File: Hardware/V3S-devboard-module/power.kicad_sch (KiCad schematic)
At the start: 68 parts, among them U101 EA3036C, U102 XC6206PxxxMR

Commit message: layout
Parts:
- removed C105, C107, C109: 18p, Capacitor_SMD:C_0402_1005Metric, symbol Device:C_Small
- removed C106, C108, C110: 10u, Capacitor_SMD:C_0603_1608Metric, symbol Device:C_Small
- removed L101, L102, L103: 2.2u, Inductor_SMD:L_1008_2520Metric, symbol Device:L_Small
- removed NT10, NT11, NT12, NT13, NT2, NT3, NT4, NT5, NT6, NT7, NT8, NT9: NetTie_2, NetTie:NetTie-2_SMD_Pad0.5mm, symbol Device:NetTie_2
- removed R101, R102, R106: 150K, Resistor_SMD:R_0402_1005Metric, symbol Device:R_Small_US
- removed R103: 200K, Resistor_SMD:R_0402_1005Metric, symbol Device:R_Small_US
- removed R104: 100K, Resistor_SMD:R_0402_1005Metric, symbol Device:R_Small_US
- removed R105: 680K, Resistor_SMD:R_0402_1005Metric, symbol Device:R_Small_US
- added C1, C3, C5: 18p, Capacitor_SMD:C_0402_1005Metric, symbol Device:C_Small
- added C2, C4, C6: 10u, Capacitor_SMD:C_0603_1608Metric, symbol Device:C_Small
- added L1, L2, L3: 2.2u, Inductor_SMD:L_1008_2520Metric, symbol Device:L_Small
- added R1: 680K, Resistor_SMD:R_0402_1005Metric, symbol Device:R_Small_US
- added R2, R5, R6: 150K, Resistor_SMD:R_0402_1005Metric, symbol Device:R_Small_US
- added R3: 200K, Resistor_SMD:R_0402_1005Metric, symbol Device:R_Small_US
- added R4: 100K, Resistor_SMD:R_0402_1005Metric, symbol Device:R_Small_US
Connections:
- net VCC_DRAM is gone; now on net 1V8: C203.2, C204.2, C205.2, C206.2, C207.2, R201.1
- net VCC_HP is gone; now on net 3V3: C224.2
- net VCC_IO is gone; now on net 3V3: C216.2, C217.2, C218.2, C219.2
- net VCC_MSCI is gone; now on net 3V3: C221.2
- net VCC_PLL is gone; now on net 3V0: C223.2
- net VCC_USB is gone; now on net 3V3: C220.2
- net VDD_CPU is gone; now on net 1V2: C212.2, C213.2, C214.2, C215.2
- net VDD_SYS is gone; now on net 1V2: C208.2, C209.2, C210.2, C211.2
- net 1V2: now also C5.2, C6.2, L3.2, R5.1
- net 1V8: now also C3.2, C4.2, L2.2, R3.1
- net 3V3: now also C1.2, C2.2, L1.2, R1.1
- net GND: now also C2.1, C4.1, C6.1, R2.2, R4.2, R6.2
- net at U101.6 (LX2): now also L1.1
- net at U101.3 (FB2): now also C5.1, R5.2, R6.1
- net at U101.11 (LX1): now also L2.1
- net at U101.14 (FB1): now also C3.1, R3.2, R4.1
- net at U101.20 (LX3): now also L3.1
- net at U101.2 (FB3): now also C1.1, R1.2, R2.1

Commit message: layout
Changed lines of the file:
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@@
 				)
 				(justify left)
-				(hide yes)
 			)
 		)
@@
 					(size 1.27 1.27)
 				)
-				(hide yes)
 			)
 		)

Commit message: layout
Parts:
- added J1: Conn_01x02, Connector_PinHeader_2.54mm:PinHeader_1x02_P2.54mm_Vertical, symbol Connector_Generic:Conn_01x02
- U101: LCSC (none) -> C570857; LCSC Part C570857 -> (none)
- U102: LCSC (none) -> C5148691
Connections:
- net 5V: now also J1.1 (Pin_1)
- net GND: now also J1.2 (Pin_2)
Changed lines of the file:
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@@
 	)
 	(symbol
+		(lib_id "Connector_Generic:Conn_01x02")
+		(at 27.94 57.15 0)
+		(mirror y)
+		(unit 1)
+		(exclude_from_sim no)
+		(in_bom yes)
+		(on_board yes)
+		(dnp no)
+		(fields_autoplaced yes)
+		(property "Reference" "J1"
+			(at 27.94 50.8 0)
+			(effects
+				(font
+					(size 1.27 1.27)
+				)
+			)
+		)
+		(property "Value" "Conn_01x02"
+			(at 27.94 53.34 0)
+			(effects
+				(font
+					(size 1.27 1.27)
+				)
+			)
+		)
+		(property "Footprint" "Connector_PinHeader_2.54mm:PinHeader_1x02_P2.54mm_Vertical"
+			(at 27.94 57.15 0)
+			(effects
+				(font
+					(size 1.27 1.27)
+				)
+				(hide yes)
+			)
+		)
+		(property "Datasheet" "~"
+			(at 27.94 57.15 0)
+			(effects
+				(font
+					(size 1.27 1.27)
+				)
+				(hide yes)
+			)
+		)
+		(property "Description" "Generic connector, single row, 01x02, script generated (kicad-library-utils/schlib/autogen/connector/)"
+			(at 27.94 57.15 0)
+			(effects
+				(font
+					(size 1.27 1.27)
+				)
+				(hide yes)
+			)
+		)
+		(pin "1"
+		)
+		(pin "2"
+		)
+		(instances
+			(project "V3S-devboard-module"
+				(path "/5d41c08e-2331-42df-a2d5-1aeb6ed4388c/5949d9b7-76b3-40a2-8931-5cd58c7934ef"
+					(reference "J1")
+					(unit 1)
+				)
+			)
+		)
+	)
+	(symbol
 		(lib_id "power:GND")
 		(at 140.97 63.5 0)
@@
 			)
 		)
+		(property "LCSC" "C5148691"
+			(at 176.53 39.37 0)
+			(effects
+				(font
+					(size 1.27 1.27)
+				)
+				(hide yes)
+			)
+		)
 		(pin "2"
 		)
@@
 	)
 	(symbol
+		(lib_id "power:VCC")
+		(at 33.02 57.15 0)
+		(unit 1)
+		(exclude_from_sim no)
+		(in_bom yes)
+		(on_board yes)
+		(dnp no)
+		(property "Reference" "#PWR0108"
+			(at 33.02 60.96 0)
+			(effects
+				(font
+					(size 1.27 1.27)
+				)
+				(hide yes)
+			)
+		)
+		(property "Value" "5V"
+			(at 31.75 53.34 0)
+			(effects
+				(font
+					(size 1.27 1.27)
+				)
+				(justify left)
+			)
+		)
+		(property "Footprint" ""
+			(at 33.02 57.15 0)
+			(effects
+				(font
+					(size 1.27 1.27)
+				)
+				(hide yes)
+			)
+		)
+		(property "Datasheet" ""
+			(at 33.02 57.15 0)
+			(effects
+				(font
+					(size 1.27 1.27)
+				)
+				(hide yes)
+			)
+		)
+		(property "Description" "Power symbol creates a global label with name \"VCC\""
+			(at 33.02 57.15 0)
+			(effects
+				(font
+					(size 1.27 1.27)
+				)
+				(hide yes)
+			)
+		)
+		(pin "1"
+		)
+		(instances
+			(project "V3S-devboard-module"
+				(path "/5d41c08e-2331-42df-a2d5-1aeb6ed4388c/5949d9b7-76b3-40a2-8931-5cd58c7934ef"
+					(reference "#PWR0108")
+					(unit 1)
+				)
+			)
+		)
+	)
+	(symbol
 		(lib_id "Device:C_Small")
 		(at 147.32 144.78 180)
@@
 	)
 	(symbol
+		(lib_id "power:GND")
+		(at 33.02 59.69 0)
+		(unit 1)
+		(exclude_from_sim no)
+		(in_bom yes)
+		(on_board yes)
+		(dnp no)
+		(fields_autoplaced yes)
+		(property "Reference" "#PWR0122"
+			(at 33.02 66.04 0)
+			(effects
+				(font
+					(size 1.27 1.27)
+				)
+				(hide yes)
+			)
+		)
+		(property "Value" "GND"
+			(at 33.02 64.77 0)
+			(effects
+				(font
+					(size 1.27 1.27)
+				)
+			)
+		)
+		(property "Footprint" ""
+			(at 33.02 59.69 0)
+			(effects
+				(font
+					(size 1.27 1.27)
+				)
+				(hide yes)
+			)
+		)
+		(property "Datasheet" ""
+			(at 33.02 59.69 0)
+			(effects
+				(font
+					(size 1.27 1.27)
+				)
+				(hide yes)
+			)
+		)
+		(property "Description" "Power symbol creates a global label with name \"GND\" , ground"
+			(at 33.02 59.69 0)
+			(effects
+				(font
+					(size 1.27 1.27)
+				)
+				(hide yes)
+			)
+		)
+		(pin "1"
+		)
+		(instances
+			(project "V3S-devboard-module"
+				(path "/5d41c08e-2331-42df-a2d5-1aeb6ed4388c/5949d9b7-76b3-40a2-8931-5cd58c7934ef"
+					(reference "#PWR0122")
+					(unit 1)
+				)
+			)
+		)
+	)
+	(symbol
 		(lib_id "Device:C_Small")
 		(at 54.61 111.76 180)
@@
 			)
 		)
-		(property "LCSC Part" "C570857"
+		(property "LCSC" "C570857"
 			(at 78.74 81.28 0)
 			(effects

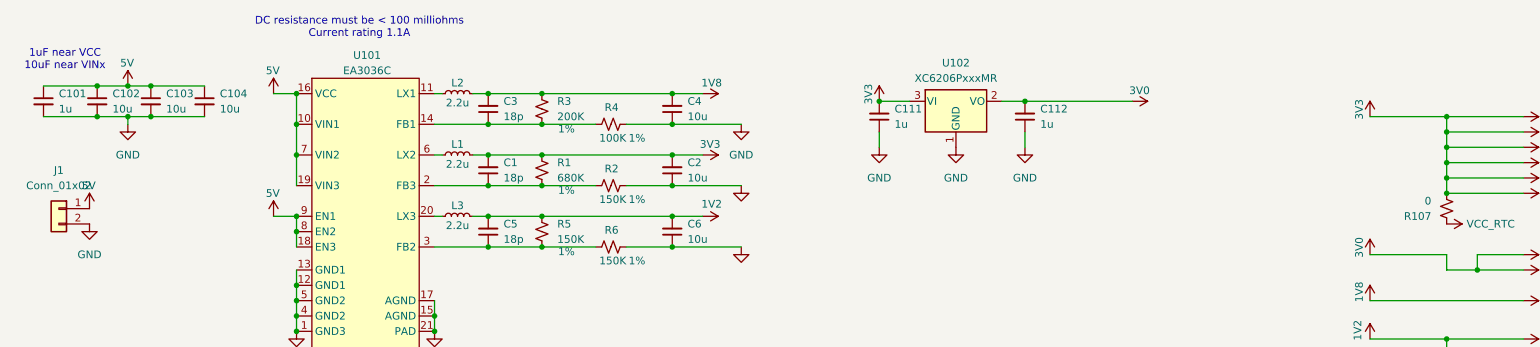
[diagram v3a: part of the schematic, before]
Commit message: re-annotated everything
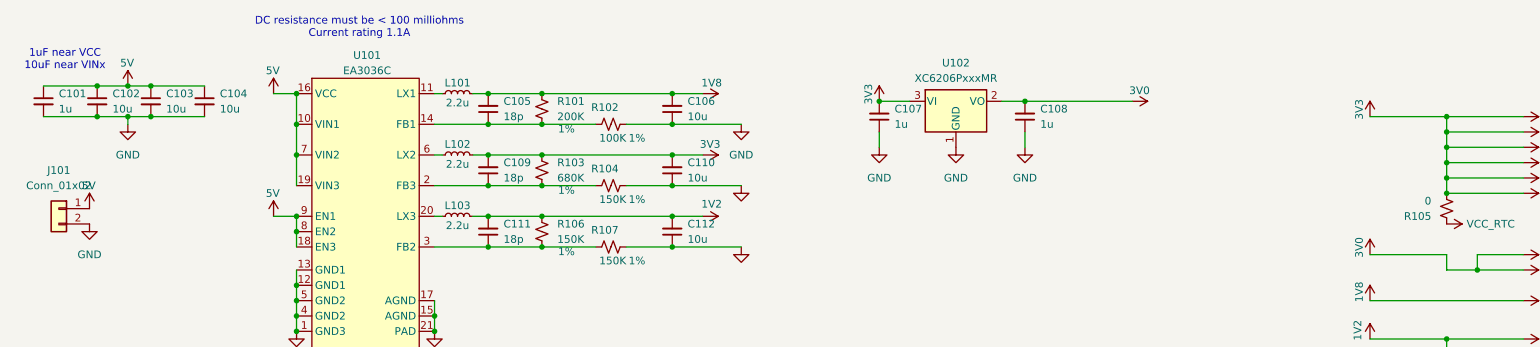
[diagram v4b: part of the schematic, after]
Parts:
- renumbered C3 to C105, C4 to C106, C111 to C107, C112 to C108, C1 to C109, C2 to C110, C5 to C111, C6 to C112, J1 to J101, L2 to L101, L1 to L102, L3 to L103, R3 to R101, R4 to R102, R1 to R103, R2 to R104, R107 to R105, R5 to R106, R6 to R107
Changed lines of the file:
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@@
 		(dnp no)
 		(fields_autoplaced yes)
-		(property "Reference" "C1"
+		(property "Reference" "C109"
 			(at 101.6 49.5235 0)
 			(effects
@@
 			(project "V3S-devboard-module"
 				(path "/5d41c08e-2331-42df-a2d5-1aeb6ed4388c/5949d9b7-76b3-40a2-8931-5cd58c7934ef"
-					(reference "C1")
+					(reference "C109")
 					(unit 1)
 				)
@@
 		(on_board yes)
 		(dnp no)
-		(property "Reference" "R3"
+		(property "Reference" "R101"
 			(at 110.49 39.3699 0)
 			(effects
@@
 			(project "V3S-devboard-module"
 				(path "/5d41c08e-2331-42df-a2d5-1aeb6ed4388c/5949d9b7-76b3-40a2-8931-5cd58c7934ef"
-					(reference "R3")
+					(reference "R101")
 					(unit 1)
 				)
@@
 		(dnp no)
 		(fields_autoplaced yes)
-		(property "Reference" "C111"
+		(property "Reference" "C107"
 			(at 166.37 40.6335 0)
 			(effects
@@
 			(project "V3S-devboard-module"
 				(path "/5d41c08e-2331-42df-a2d5-1aeb6ed4388c/5949d9b7-76b3-40a2-8931-5cd58c7934ef"
-					(reference "C111")
+					(reference "C107")
 					(unit 1)
 				)
@@
 		(on_board yes)
 		(dnp no)
-		(property "Reference" "R5"
+		(property "Reference" "R106"
 			(at 110.49 59.6899 0)
 			(effects
@@
 			(project "V3S-devboard-module"
 				(path "/5d41c08e-2331-42df-a2d5-1aeb6ed4388c/5949d9b7-76b3-40a2-8931-5cd58c7934ef"
-					(reference "R5")
+					(reference "R106")
 					(unit 1)
 				)
@@
 		(dnp no)
 		(fields_autoplaced yes)
-		(property "Reference" "J1"
+		(property "Reference" "J101"
 			(at 27.94 50.8 0)
 			(effects
@@
 			(project "V3S-devboard-module"
 				(path "/5d41c08e-2331-42df-a2d5-1aeb6ed4388c/5949d9b7-76b3-40a2-8931-5cd58c7934ef"
-					(reference "J1")
+					(reference "J101")
 					(unit 1)
 				)
@@
 		(on_board yes)
 		(dnp no)
-		(property "Reference" "R6"
+		(property "Reference" "R107"
 			(at 120.65 60.706 90)
 			(effects
@@
 			(project "V3S-devboard-module"
 				(path "/5d41c08e-2331-42df-a2d5-1aeb6ed4388c/5949d9b7-76b3-40a2-8931-5cd58c7934ef"
-					(reference "R6")
+					(reference "R107")
 					(unit 1)
 				)
@@
 		(on_board yes)
 		(dnp no)
-		(property "Reference" "R1"
+		(property "Reference" "R103"
 			(at 110.49 49.5299 0)
 			(effects
@@
 			(project "V3S-devboard-module"
 				(path "/5d41c08e-2331-42df-a2d5-1aeb6ed4388c/5949d9b7-76b3-40a2-8931-5cd58c7934ef"
-					(reference "R1")
+					(reference "R103")
 					(unit 1)
 				)
@@
 		(dnp no)
 		(fields_autoplaced yes)
-		(property "Reference" "C2"
+		(property "Reference" "C110"
 			(at 132.08 49.5235 0)
 			(effects
@@
 			(project "V3S-devboard-module"
 				(path "/5d41c08e-2331-42df-a2d5-1aeb6ed4388c/5949d9b7-76b3-40a2-8931-5cd58c7934ef"
-					(reference "C2")
+					(reference "C110")
 					(unit 1)
 				)
@@
 		(on_board yes)
 		(dnp no)
-		(property "Reference" "L3"
+		(property "Reference" "L103"
 			(at 93.98 56.642 90)
 			(effects
@@
 			(project "V3S-devboard-module"
 				(path "/5d41c08e-2331-42df-a2d5-1aeb6ed4388c/5949d9b7-76b3-40a2-8931-5cd58c7934ef"
-					(reference "L3")
+					(reference "L103")
 					(unit 1)
 				)
@@
 		(on_board yes)
 		(dnp no)
-		(property "Reference" "R2"
+		(property "Reference" "R104"
 			(at 120.65 50.546 90)
 			(effects
@@
 			(project "V3S-devboard-module"
 				(path "/5d41c08e-2331-42df-a2d5-1aeb6ed4388c/5949d9b7-76b3-40a2-8931-5cd58c7934ef"
-					(reference "R2")
+					(reference "R104")
 					(unit 1)
 				)
@@
 		(dnp no)
 		(fields_autoplaced yes)
-		(property "Reference" "C4"
+		(property "Reference" "C106"
 			(at 132.08 39.3635 0)
 			(effects
@@
 			(project "V3S-devboard-module"
 				(path "/5d41c08e-2331-42df-a2d5-1aeb6ed4388c/5949d9b7-76b3-40a2-8931-5cd58c7934ef"
-					(reference "C4")
+					(reference "C106")
 					(unit 1)
 				)
@@
 		(on_board yes)
 		(dnp no)
-		(property "Reference" "R107"
+		(property "Reference" "R105"
 			(at 255.27 58.4201 0)
 			(effects
@@
 			(project "V3S-devboard-module"
 				(path "/5d41c08e-2331-42df-a2d5-1aeb6ed4388c/5949d9b7-76b3-40a2-8931-5cd58c7934ef"
-					(reference "R107")
+					(reference "R105")
 					(unit 1)
 				)
@@
 		(on_board yes)
 		(dnp no)
-		(property "Reference" "L2"
+		(property "Reference" "L101"
 			(at 93.98 36.322 90)
 			(effects
@@
 			(project "V3S-devboard-module"
 				(path "/5d41c08e-2331-42df-a2d5-1aeb6ed4388c/5949d9b7-76b3-40a2-8931-5cd58c7934ef"
-					(reference "L2")
+					(reference "L101")
 					(unit 1)
 				)
@@
 		(dnp no)
 		(fields_autoplaced yes)
-		(property "Reference" "C6"
+		(property "Reference" "C112"
 			(at 132.08 59.6835 0)
 			(effects
@@
 			(project "V3S-devboard-module"
 				(path "/5d41c08e-2331-42df-a2d5-1aeb6ed4388c/5949d9b7-76b3-40a2-8931-5cd58c7934ef"
-					(reference "C6")
+					(reference "C112")
 					(unit 1)
 				)
@@
 		(dnp no)
 		(fields_autoplaced yes)
-		(property "Reference" "C3"
+		(property "Reference" "C105"
 			(at 101.6 39.3635 0)
 			(effects
@@
 			(project "V3S-devboard-module"
 				(path "/5d41c08e-2331-42df-a2d5-1aeb6ed4388c/5949d9b7-76b3-40a2-8931-5cd58c7934ef"
-					(reference "C3")
+					(reference "C105")
 					(unit 1)
 				)
@@
 		(on_board yes)
 		(dnp no)
-		(property "Reference" "L1"
+		(property "Reference" "L102"
 			(at 93.98 46.482 90)
 			(effects
@@
 			(project "V3S-devboard-module"
 				(path "/5d41c08e-2331-42df-a2d5-1aeb6ed4388c/5949d9b7-76b3-40a2-8931-5cd58c7934ef"
-					(reference "L1")
+					(reference "L102")
 					(unit 1)
 				)
@@
 		(dnp no)
 		(fields_autoplaced yes)
-		(property "Reference" "C5"
+		(property "Reference" "C111"
 			(at 101.6 59.6835 0)
 			(effects
@@
 			(project "V3S-devboard-module"
 				(path "/5d41c08e-2331-42df-a2d5-1aeb6ed4388c/5949d9b7-76b3-40a2-8931-5cd58c7934ef"
-					(reference "C5")
+					(reference "C111")
 					(unit 1)
 				)
@@
 		(dnp no)
 		(fields_autoplaced yes)
-		(property "Reference" "C112"
+		(property "Reference" "C108"
 			(at 190.5 40.6335 0)
 			(effects
@@
 			(project "V3S-devboard-module"
 				(path "/5d41c08e-2331-42df-a2d5-1aeb6ed4388c/5949d9b7-76b3-40a2-8931-5cd58c7934ef"
-					(reference "C112")
+					(reference "C108")
 					(unit 1)
 				)
@@
 		(on_board yes)
 		(dnp no)
-		(property "Reference" "R4"
+		(property "Reference" "R102"
 			(at 120.65 40.386 90)
 			(effects
@@
 			(project "V3S-devboard-module"
 				(path "/5d41c08e-2331-42df-a2d5-1aeb6ed4388c/5949d9b7-76b3-40a2-8931-5cd58c7934ef"
-					(reference "R4")
+					(reference "R102")
 					(unit 1)
 				)

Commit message: pre production tests
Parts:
- C101, C204, C206, C209, C213, C217, C225: LCSC (none) -> C5673
- C102, C103, C104, C203, C208, C212, C216, C227: LCSC (none) -> C1691
- C105: LCSC (none) -> C541431
- C106: renamed from C107; LCSC (none) -> C5673
- C107: renamed from C108; LCSC (none) -> C5673
- C108: renamed from C109; LCSC (none) -> C541431
- C109: renamed from C110; LCSC (none) -> C1691
- C110: renamed from C111; LCSC (none) -> C541431
- C111: renamed from C112; LCSC (none) -> C1691
- C201, C202, C205, C207, C210, C211, C214, C215, C218, C219, C220, C221, C222, C223, C224, C228: LCSC (none) -> C1525
- C226, C229: LCSC (none) -> C1705
- Ce101: renamed from C106; LCSC (none) -> C1691
- J101: now not fitted; now left out of the parts list
- L101, L102, L103: LCSC (none) -> C86092
- R101, R203: LCSC (none) -> C114763
- R102: LCSC (none) -> C60491
- R103: LCSC (none) -> C163456
- R104, R106, R107: LCSC (none) -> C93947
- R105: LCSC (none) -> C106231
- R201, R202: LCSC (none) -> C60488

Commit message: working on final touches
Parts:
- added D101: LED, LED_SMD:LED_0603_1608Metric, symbol Device:LED
- added R108: 1K, Resistor_SMD:R_0402_1005Metric, symbol Device:R_Small_US
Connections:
- net 5V: now also R108.1
- net GND: now also D101.1 (K)
- new net: D101.2 (A), R108.2

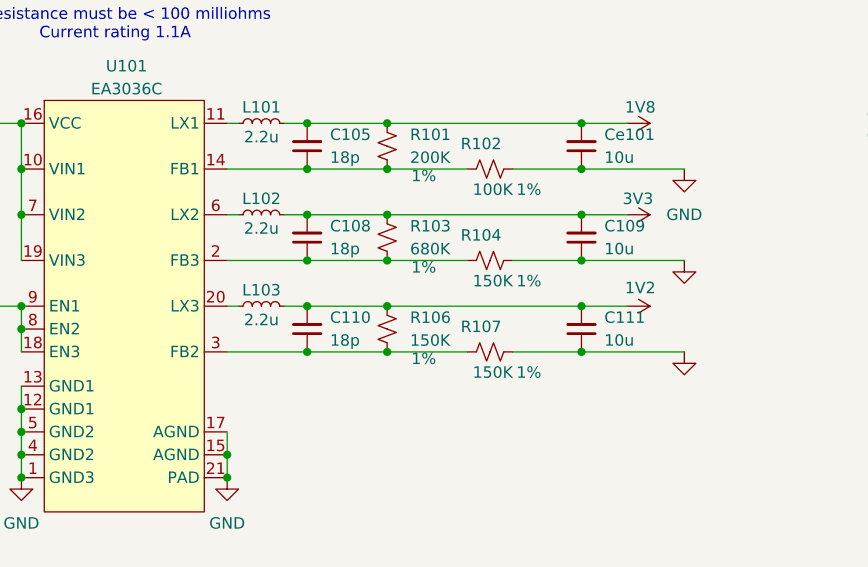
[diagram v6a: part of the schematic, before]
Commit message: wrong order of pins of regulator
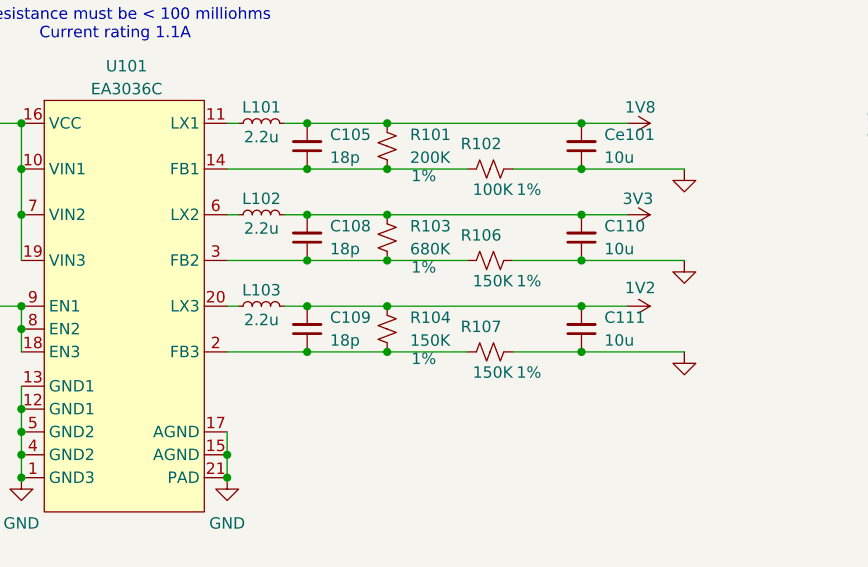
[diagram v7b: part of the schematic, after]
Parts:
- C109: value 10u -> 18p; footprint Capacitor_SMD:C_0603_1608Metric -> Capacitor_SMD:C_0402_1005Metric; LCSC C1691 -> C541431
- C110: value 18p -> 10u; footprint Capacitor_SMD:C_0402_1005Metric -> Capacitor_SMD:C_0603_1608Metric; LCSC C541431 -> C1691
- U101: LCSC Part (none) -> C570857
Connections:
- net 1V2: now also C109.2, R104.1; no longer C110.2, R106.1
- net 3V3: now also C110.2; no longer C109.2
- net GND: now also C110.1, R106.2; no longer C109.1, R104.2
- net at C108.1, R103.2: now also R106.1, U101.3 (FB2); no longer R104.1, U101.2 (FB3)
- new net: C109.1, R104.2, R107.1, U101.2 (FB3)
